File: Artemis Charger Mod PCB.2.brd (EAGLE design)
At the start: 95.9 x 94.6 mm, 159 parts, among them J1 MOLEX_CLICKMATE-2-VERTICAL, J2 MOLEX_CLICKMATE-4-VERTICAL, J3 MOLEX_CLICKMATE-2-VERTICAL, J4 MOLEX_CLICKMATE-2-VERTICAL, J5 MOLEX_CLICKMATE-2-VERTICAL, J6 MOLEX_CLICKMATE-2-VERTICAL, Q10 BSS138, Q11 BSS138, Q8 BSS138, Q9 BSS138, U10 TPS562219, U11 ISO7340, U12 ISO7340, U13 TPS562219, U14 MCP2515-TSSOP, U15 MCP2562, U17 CD4050BD, U18 CD4043B, U19 SN74LVC08ASOIC, U20 SN74LVC32ASOIC, U22 LTC1155, U23 CSD17506Q5A, U26 CSD17506Q5A, U27 LTC1155, U28 CSD17506Q5A, U29 LTC1155, U3 MAX5812, U30 CSD17506Q5A, U32 CSD17506Q5A, U34 CSD17506Q5A, U49 TL7712A-SOIC, U8 MAX5812, U9 TPS562219

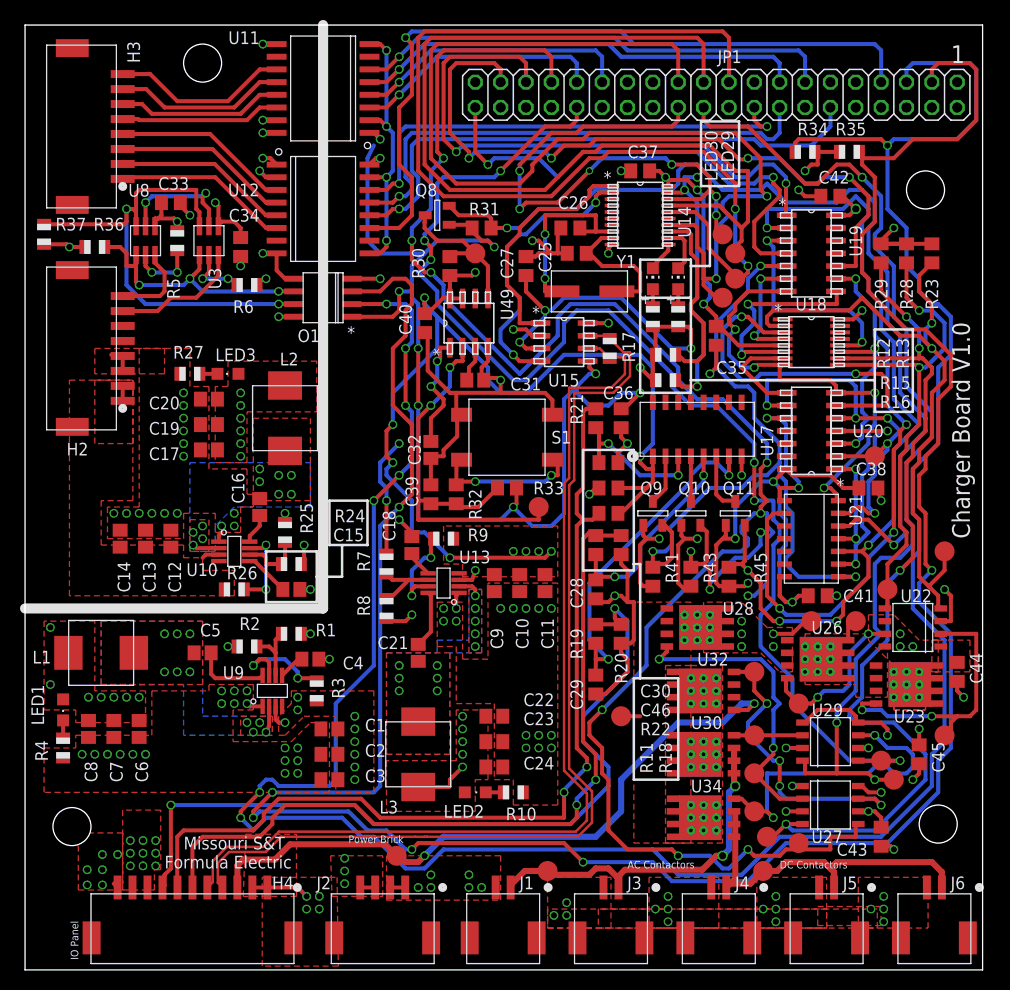
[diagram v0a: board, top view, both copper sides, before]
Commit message: Fixed crooked supply planes, moved planes away from isolation line, made better silkscreens, about to do BOM
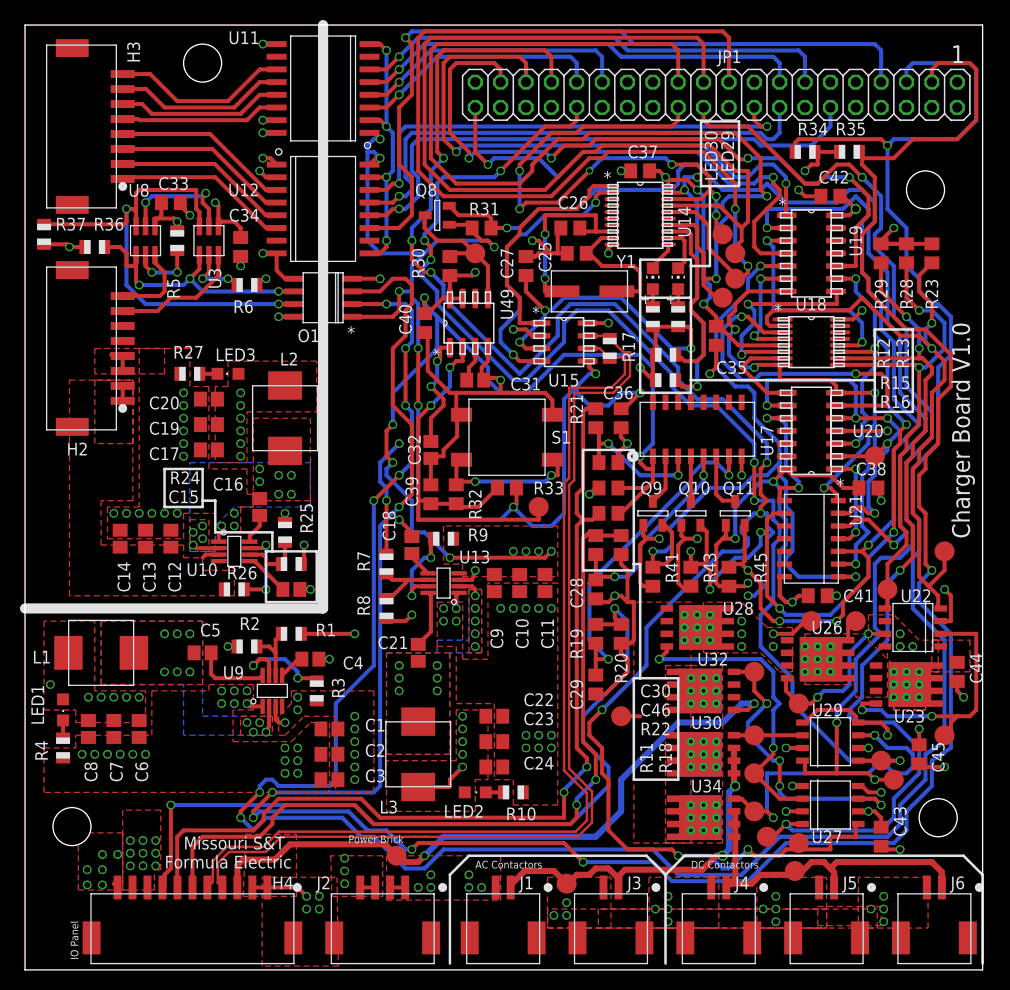
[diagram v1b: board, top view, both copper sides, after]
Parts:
- moved TP16 3.17 mm to (76.5, -4.70)
- moved TP9 2.29 mm to (53.6, -5.97)
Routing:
- net +3V3: track 235.3 -> 242.7 mm, vias 36 -> 35
- net GND1: track 191.7 -> 193.2 mm
- net RTDS_SOURCE1: track 36.3 -> 37.1 mm
- net SCL1_I2C: track 249.7 -> 250.3 mm
- net SDA1_I2C: track 253.8 -> 254.4 mm

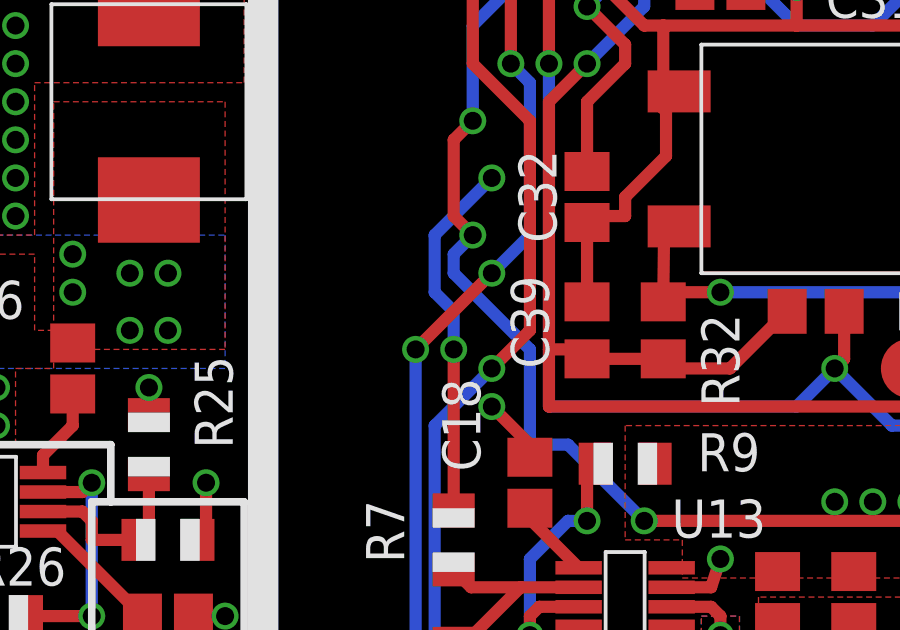
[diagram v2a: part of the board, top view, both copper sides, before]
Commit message: Changes supply Plane
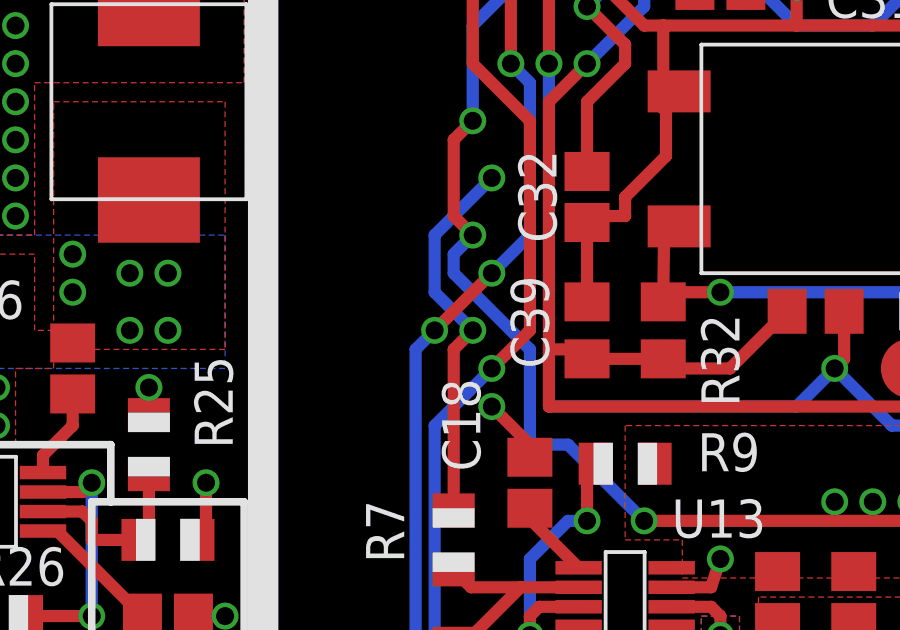
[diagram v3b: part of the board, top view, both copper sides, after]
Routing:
- net +5V/1: track 68.0 -> 68.5 mm
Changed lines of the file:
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@@
 <setting verticaltext="up"/>
 </settings>
-<grid distance="0.01" unitdist="mm" unit="mm" style="lines" multiple="1" display="yes" altdistance="0.0125" altunitdist="inch" altunit="inch"/>
+<grid distance="0.025" unitdist="inch" unit="inch" style="lines" multiple="1" display="yes" altdistance="0.0125" altunitdist="inch" altunit="inch"/>
 <layers>
 <layer number="1" name="Top" color="4" fill="1" visible="yes" active="yes"/>
@@
 <layer number="13" name="Route13" color="4" fill="5" visible="no" active="no"/>
 <layer number="14" name="Route14" color="1" fill="6" visible="no" active="no"/>
-<layer number="15" name="Route15" color="13" fill="1" visible="no" active="yes"/>
+<layer number="15" name="Route15" color="13" fill="1" visible="yes" active="yes"/>
 <layer number="16" name="Bottom" color="1" fill="1" visible="yes" active="yes"/>
 <layer number="17" name="Pads" color="2" fill="1" visible="yes" active="yes"/>
@@
 <vertex x="0" y="19.05"/>
 <vertex x="31.75" y="19.05"/>
-<vertex x="31.75" y="28.575"/>
-<vertex x="30.48" y="29.845"/>
-<vertex x="30.48" y="35.56"/>
-<vertex x="31.75" y="36.83"/>
 <vertex x="31.75" y="47.625"/>
 <vertex x="33.02" y="48.895"/>
@@
 </polygon>
 <wire x1="90.17" y1="69.85" x2="92.71" y2="69.85" width="0.4064" layer="15"/>
-<wire x1="35.56" y1="27.035" x2="35.56" y2="32.385" width="0.4064" layer="1"/>
-<via x="35.56" y="32.385" extent="1-16" drill="0.6"/>
-<wire x1="35.56" y1="32.385" x2="35.56" y2="33.655" width="0.4064" layer="16"/>
-<wire x1="35.56" y1="33.655" x2="34.925" y2="34.29" width="0.4064" layer="16"/>
+<via x="36.195" y="33.02" extent="1-16" drill="0.6"/>
+<wire x1="36.195" y1="33.02" x2="34.925" y2="34.29" width="0.4064" layer="16"/>
 <wire x1="34.925" y1="34.29" x2="34.925" y2="36.195" width="0.4064" layer="16"/>
 <wire x1="34.925" y1="36.195" x2="36.83" y2="38.1" width="0.4064" layer="16"/>
 <via x="36.83" y="38.1" extent="1-16" drill="0.6"/>
+<wire x1="35.56" y1="27.035" x2="35.56" y2="32.385" width="0.4064" layer="1"/>
+<wire x1="35.56" y1="32.385" x2="36.195" y2="33.02" width="0.4064" layer="1"/>
 </signal>
 <signal name="SCL">
@@
 <wire x1="35.56" y1="52.07" x2="37.465" y2="52.07" width="0.4064" layer="16"/>
 <wire x1="37.465" y1="52.07" x2="38.1" y2="51.435" width="0.4064" layer="16"/>
-<wire x1="34.29" y1="32.385" x2="34.29" y2="15.875" width="0.4064" layer="16"/>
 <wire x1="34.29" y1="15.875" x2="30.48" y2="12.065" width="0.4064" layer="16"/>
 <wire x1="30.48" y1="12.065" x2="30.48" y2="4.445" width="0.4064" layer="16"/>
@@
 <wire x1="38.1" y1="36.195" x2="36.83" y2="34.925" width="0.4064" layer="16"/>
 <via x="36.83" y="34.925" extent="1-16" drill="0.6"/>
-<wire x1="36.83" y1="34.925" x2="34.29" y2="32.385" width="0.4064" layer="1"/>
-<via x="34.29" y="32.385" extent="1-16" drill="0.6"/>
+<via x="34.925" y="33.02" extent="1-16" drill="0.6"/>
 <wire x1="87.63" y1="55.88" x2="88.9" y2="54.61" width="0.4064" layer="16"/>
 <wire x1="88.9" y1="54.61" x2="88.9" y2="53.34" width="0.4064" layer="16"/>
@@
 <wire x1="86.995" y1="0" x2="86.995" y2="1.905" width="0.4064" layer="16"/>
 <wire x1="86.995" y1="1.905" x2="89.535" y2="4.445" width="0.4064" layer="16"/>
+<wire x1="34.29" y1="32.385" x2="34.29" y2="15.875" width="0.4064" layer="16"/>
+<wire x1="34.925" y1="33.02" x2="36.83" y2="34.925" width="0.4064" layer="1"/>
+<wire x1="34.925" y1="33.02" x2="34.29" y2="32.385" width="0.4064" layer="16"/>
 </signal>
 <signal name="FET_CONNECT_1">

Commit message: Added STENCIL
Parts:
- U3, U8: value MAX5812 -> MAX5812LEUT+TCT-ND
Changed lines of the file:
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@@
 <layer number="13" name="Route13" color="4" fill="5" visible="no" active="no"/>
 <layer number="14" name="Route14" color="1" fill="6" visible="no" active="no"/>
-<layer number="15" name="Route15" color="13" fill="1" visible="yes" active="yes"/>
+<layer number="15" name="Route15" color="13" fill="1" visible="no" active="yes"/>
 <layer number="16" name="Bottom" color="1" fill="1" visible="yes" active="yes"/>
 <layer number="17" name="Pads" color="2" fill="1" visible="yes" active="yes"/>
@@
 <element name="H2" library="FormE" package="MOLEX-CLIKMATE-8-VERTICAL-HEADER" value="MOLEX_CLIKMATE-8-VERTICAL" x="5.08" y="47.625" smashed="yes" rot="R270">
 <attribute name="NAME" x="3.525" y="36.909" size="1.27" layer="25" font="vector"/>
+<attribute name="PARTNO" value="5025840870" x="5.08" y="47.625" size="1.778" layer="27" rot="R270" display="off"/>
 </element>
 <element name="JP1" library="pinhead" package="2X20" value="" x="68.58" y="73.025" smashed="yes" rot="R180">
@@
 <attribute name="VALUE" x="17.07" y="24.055" size="1.27" layer="27"/>
 </element>
-<element name="U3" library="FormE" package="MAX5812" value="MAX5812" x="17.78" y="58.42" smashed="yes" rot="R270">
+<element name="U3" library="FormE" package="MAX5812" value="MAX5812LEUT+TCT-ND" x="17.78" y="58.42" smashed="yes" rot="R270">
 <attribute name="NAME" x="17.74" y="55.705" size="1.27" layer="25" font="vector" rot="R270"/>
 <attribute name="PARTNO" value="MAX5812LEUT+T" x="17.78" y="58.42" size="1.778" layer="27" rot="R270" display="off"/>
 </element>
-<element name="U8" library="FormE" package="MAX5812" value="MAX5812" x="11.43" y="58.42" smashed="yes" rot="R270">
+<element name="U8" library="FormE" package="MAX5812" value="MAX5812LEUT+TCT-ND" x="11.43" y="58.42" smashed="yes" rot="R270">
 <attribute name="NAME" x="9.7" y="62.825" size="1.27" layer="25" font="vector"/>
 <attribute name="PARTNO" value="MAX5812LEUT+T" x="11.43" y="58.42" size="1.778" layer="27" rot="R270" display="off"/>
@@
 <element name="J2" library="FormE" package="MOLEX-CLIKMATE-4-VERTICAL-HEADER" value="MOLEX_CLICKMATE-4-VERTICAL" x="35.179" y="-10.414" smashed="yes">
 <attribute name="NAME" x="28.544" y="-6.525" size="1.27" layer="25" font="vector"/>
+<attribute name="PARTNO" value="5040500491" x="35.179" y="-10.414" size="1.778" layer="27" display="off"/>
 </element>
 <element name="U11" library="FormE" package="ISO734X" value="ISO7340" x="29.21" y="73.66" smashed="yes" rot="R180">
@@
 <element name="H3" library="FormE" package="MOLEX-CLIKMATE-8-VERTICAL-HEADER" value="MOLEX_CLIKMATE-8-VERTICAL" x="5.08" y="69.85" smashed="yes" rot="R270">
 <attribute name="NAME" x="9.604" y="78.39" size="1.27" layer="25" font="vector" rot="R270"/>
+<attribute name="PARTNO" value="5025840870" x="5.08" y="69.85" size="1.778" layer="27" rot="R270" display="off"/>
 </element>
 <element name="U14" library="FormE" package="TSSOP20_MC" value="MCP2515-TSSOP" x="60.96" y="60.96" smashed="yes">
@@
 <element name="H4" library="FormE" package="MOLEX_CLICKMATE-11-VERTICAL-HEADER" value="" x="16.129" y="-10.414" smashed="yes">
 <attribute name="NAME" x="24.099" y="-6.525" size="1.27" layer="25" font="vector"/>
+<attribute name="PARTNO" value="5025841170" x="16.129" y="-10.414" size="1.778" layer="27" display="off"/>
 </element>
 <element name="R11" library="rcl" package="R0805" value="0" x="56.515" y="27.94" smashed="yes" rot="R90">
@@
 <element name="J1" library="FormE" package="MOLEX-CLIKMATE-2-VERTICAL-HEADER" value="MOLEX_CLICKMATE-2-VERTICAL" x="47.244" y="-10.414" smashed="yes">
 <attribute name="NAME" x="48.864" y="-6.525" size="1.27" layer="25" font="vector"/>
+<attribute name="PARTNO" value="5025840270" x="47.244" y="-10.414" size="1.778" layer="27" display="off"/>
 </element>
 <element name="J3" library="FormE" package="MOLEX-CLIKMATE-2-VERTICAL-HEADER" value="MOLEX_CLICKMATE-2-VERTICAL" x="58.039" y="-10.414" smashed="yes">
 <attribute name="NAME" x="59.659" y="-6.525" size="1.27" layer="25" font="vector"/>
+<attribute name="PARTNO" value="5025840270" x="58.039" y="-10.414" size="1.778" layer="27" display="off"/>
 </element>
 <element name="J4" library="FormE" package="MOLEX-CLIKMATE-2-VERTICAL-HEADER" value="MOLEX_CLICKMATE-2-VERTICAL" x="68.834" y="-10.414" smashed="yes">
 <attribute name="NAME" x="70.454" y="-6.525" size="1.27" layer="25" font="vector"/>
+<attribute name="PARTNO" value="5025840270" x="68.834" y="-10.414" size="1.778" layer="27" display="off"/>
 </element>
 <element name="J5" library="FormE" package="MOLEX-CLIKMATE-2-VERTICAL-HEADER" value="MOLEX_CLICKMATE-2-VERTICAL" x="79.629" y="-10.414" smashed="yes">
 <attribute name="NAME" x="81.249" y="-6.525" size="1.27" layer="25"/>
+<attribute name="PARTNO" value="5025840270" x="79.629" y="-10.414" size="1.778" layer="27" display="off"/>
 </element>
 <element name="R34" library="adafruit" package="R0805" value="10K" x="77.47" y="67.31" smashed="yes" rot="R180">
@@
 <element name="J6" library="FormE" package="MOLEX-CLIKMATE-2-VERTICAL-HEADER" value="MOLEX_CLICKMATE-2-VERTICAL" x="90.424" y="-10.414" smashed="yes">
 <attribute name="NAME" x="92.044" y="-6.525" size="1.27" layer="25"/>
+<attribute name="PARTNO" value="5025840270" x="90.424" y="-10.414" size="1.778" layer="27" display="off"/>
 </element>
 </elements>
